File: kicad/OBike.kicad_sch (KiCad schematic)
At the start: 48 parts, among them J1 Conn_01x08, J2 Micro_SD_Card_Det1, J3 Conn_01x02, J4 2337019-1, J6 Conn_01x02, SW1 5_position_tactile, U1 DPS368XTSA1, U2 DS3231M, U3 MCP23017_SO, U4 74HC14, U5 Seeed Studio XIAO SAMD21, U6 MAX-M8C-0

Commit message: gps 4-layer
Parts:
- removed J4: 2337019-1, TE Connectivity:TE_2337019-1, symbol TE Connectivity:2337019-1
- added AE1: Antenna, Antenna:AC30036-01, symbol Device:Antenna
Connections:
- net ANT: now also AE1.1 (A)
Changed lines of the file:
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@@
 	(wire
 		(pts
-			(xy 96.52 102.87) (xy 99.06 102.87)
+			(xy 96.52 110.49) (xy 99.06 110.49)
 		)
 		(stroke
@@
 	(wire
 		(pts
-			(xy 99.06 105.41) (xy 99.06 107.95)
-		)
-		(stroke
-			(width 0)
-			(type default)
-		)
-	)
-	(wire
-		(pts
 			(xy 195.58 33.02) (xy 193.04 33.02)
 		)
@@
 	(wire
 		(pts
-			(xy 96.52 105.41) (xy 99.06 105.41)
-		)
-		(stroke
-			(width 0)
-			(type default)
-		)
-	)
-	(wire
-		(pts
 			(xy 247.65 146.05) (xy 247.65 160.02)
 		)
@@
 	(global_label "ANT"
 		(shape input)
-		(at 99.06 102.87 0)
+		(at 99.06 110.49 0)
 		(fields_autoplaced yes)
 		(effects
@@
 		)
 		(property "Intersheetrefs" "${INTERSHEET_REFS}"
-			(at 105.4319 102.87 0)
+			(at 105.4319 110.49 0)
 			(effects
 				(font
@@
 	)
 	(symbol
-		(lib_id "power:Earth")
-		(at 99.06 107.95 0)
-		(unit 1)
-		(exclude_from_sim no)
-		(in_bom yes)
-		(on_board yes)
-		(dnp no)
-		(property "Reference" "#PWR019"
-			(at 99.06 114.3 0)
-			(effects
-				(font
-					(size 1.27 1.27)
-				)
-				(hide yes)
-			)
-		)
-		(property "Value" "GND"
-			(at 101.6 109.2199 0)
-			(effects
-				(font
-					(size 1.27 1.27)
-				)
-				(justify left)
-			)
-		)
-		(property "Footprint" ""
-			(at 99.06 107.95 0)
-			(effects
-				(font
-					(size 1.27 1.27)
-				)
-				(hide yes)
-			)
-		)
-		(property "Datasheet" "~"
-			(at 99.06 107.95 0)
-			(effects
-				(font
-					(size 1.27 1.27)
-				)
-				(hide yes)
-			)
-		)
-		(property "Description" "Power symbol creates a global label with name \"Earth\""
-			(at 99.06 107.95 0)
-			(effects
-				(font
-					(size 1.27 1.27)
-				)
-				(hide yes)
-			)
-		)
-		(pin "1"
-		)
-		(instances
-			(project "OBike"
-				(path "/b6c91502-91b9-44d0-9569-7774925b5f71"
-					(reference "#PWR019")
-					(unit 1)
-				)
-			)
-		)
-	)
-	(symbol
 		(lib_id "Device:R")
 		(at 199.39 36.83 270)
@@
 	)
 	(symbol
+		(lib_id "Device:Antenna")
+		(at 91.44 110.49 90)
+		(unit 1)
+		(exclude_from_sim no)
+		(in_bom yes)
+		(on_board yes)
+		(dnp no)
+		(fields_autoplaced yes)
+		(property "Reference" "AE1"
+			(at 92.075 104.14 90)
+			(effects
+				(font
+					(size 1.27 1.27)
+				)
+			)
+		)
+		(property "Value" "Antenna"
+			(at 92.075 106.68 90)
+			(effects
+				(font
+					(size 1.27 1.27)
+				)
+			)
+		)
+		(property "Footprint" "Antenna:AC30036-01"
+			(at 91.44 110.49 0)
+			(effects
+				(font
+					(size 1.27 1.27)
+				)
+				(hide yes)
+			)
+		)
+		(property "Datasheet" "~"
+			(at 91.44 110.49 0)
+			(effects
+				(font
+					(size 1.27 1.27)
+				)
+				(hide yes)
+			)
+		)
+		(property "Description" "Antenna"
+			(at 91.44 110.49 0)
+			(effects
+				(font
+					(size 1.27 1.27)
+				)
+				(hide yes)
+			)
+		)
+		(pin "1"
+		)
+		(instances
+			(project ""
+				(path "/b6c91502-91b9-44d0-9569-7774925b5f71"
+					(reference "AE1")
+					(unit 1)
+				)
+			)
+		)
+	)
+	(symbol
 		(lib_id "Device:R")
 		(at 193.04 27.94 0)
@@
 					(unit 1)
 				)
-			)
-		)
-	)
-	(symbol
-		(lib_id "TE Connectivity:2337019-1")
-		(at 93.98 102.87 0)
-		(unit 1)
-		(exclude_from_sim no)
-		(in_bom yes)
-		(on_board yes)
-		(dnp no)
-		(fields_autoplaced yes)
-		(property "Reference" "J4"
-			(at 92.9005 96.52 0)
-			(effects
-				(font
-					(size 1.27 1.27)
-				)
-			)
-		)
-		(property "Value" "2337019-1"
-			(at 92.9005 99.06 0)
-			(effects
-				(font
-					(size 1.27 1.27)
-				)
-			)
-		)
-		(property "Footprint" "TE Connectivity:TE_2337019-1"
-			(at 93.98 102.87 0)
-			(effects
-				(font
-					(size 1.27 1.27)
-				)
-				(justify bottom)
-				(hide yes)
-			)
-		)
-		(property "Datasheet" ""
-			(at 93.98 102.87 0)
-			(effects
-				(font
-					(size 1.27 1.27)
-				)
-				(hide yes)
-			)
-		)
-		(property "Description" ""
-			(at 93.98 102.87 0)
-			(effects
-				(font
-					(size 1.27 1.27)
-				)
-				(hide yes)
-			)
-		)
-		(property "PARTREV" "A4"
-			(at 93.98 102.87 0)
-			(effects
-				(font
-					(size 1.27 1.27)
-				)
-				(justify bottom)
-				(hide yes)
-			)
-		)
-		(property "STANDARD" "Manufacturer Recommendations"
-			(at 93.98 102.87 0)
-			(effects
-				(font
-					(size 1.27 1.27)
-				)
-				(justify bottom)
-				(hide yes)
-			)
-		)
-		(property "MAXIMUM_PACKAGE_HEIGHT" "1.25mm"
-			(at 93.98 102.87 0)
-			(effects
-				(font
-					(size 1.27 1.27)
-				)
-				(justify bottom)
-				(hide yes)
-			)
-		)
-		(property "MANUFACTURER" "TE Connectivity"
-			(at 93.98 102.87 0)
-			(effects
-				(font
-					(size 1.27 1.27)
-				)
-				(justify bottom)
-				(hide yes)
-			)
-		)
-		(pin "G1"
-		)
-		(pin "1"
-		)
-		(instances
-			(project ""
-				(path "/b6c91502-91b9-44d0-9569-7774925b5f71"
-					(reference "J4")
-					(unit 1)
-				)

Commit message: stopper using logger
also some fixes for tcx
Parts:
- added R15, R17: 100K, Resistor_SMD:R_0603_1608Metric, symbol Device:R
- AE1: Digikiey PN (none) -> 5350-AC30036-01-ND; Manufacturer (none) -> The Antenna Company; Manufacturer PN (none) -> AC30036-01
- D1, D2, D3, D4, D5: Digikiey PN (none) -> 1N4148WRHGCT-ND; Manufacturer (none) -> Taiwan Semiconductor Corporation; Manufacturer PN (none) -> 1N4148W RHG
- J2: Digikiey PN (none) -> 2223-MSD-11-ACT-ND; Manufacturer (none) -> Same Sky (Formerly CUI Devices); Manufacturer PN (none) -> MSD-11-A
- J3: Digikiey PN (none) -> 455-1719-ND; Manufacturer (none) -> JST Sales America Inc.; Manufacturer PN (none) -> CONN HEADER R/A 2POS 2MM
- R16: value 10K -> 100K
- SW1: Digikiey PN (none) -> 450-2425755-1CT-ND; Manufacturer (none) -> TE Connectivity ALCOSWITCH Switches; Manufacturer PN (none) -> 2425755-1
- U1: Digikiey PN (none) -> DPS368XTSA1CT-ND; Manufacturer (none) -> Infineon Technologies; Manufacturer PN (none) -> DPS368XTSA1
- U2: Digikiey PN (none) -> DS3231MZ+-ND; Manufacturer (none) -> Analog Devices Inc./Maxim Integrated; Manufacturer PN (none) -> DS3231MZ+
- U3: Digikiey PN (none) -> MCP23017T-E/SOCT-ND; Manufacturer (none) -> Microchip Technology; Manufacturer PN (none) -> MCP23017T-E/SO
- U4: Digikiey PN (none) -> 74HC14DCT-ND; Manufacturer (none) -> Toshiba Semiconductor and Storage; Manufacturer PN (none) -> 74HC14D
- U6: Digikiey PN (none) -> 672-MAX-M8C-0CT-ND; MANUFACTURER u-blox -> (none); Manufacturer (none) -> u-blox; Manufacturer PN (none) -> MAX-M8C-0
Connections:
- net at C10.1, J2.1 (DAT2), R11.1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: now also R15.1, R17.1; no longer J2.4 (VDD), J2.8 (DAT1)
- new net: J2.4 (VDD), R15.2
- new net: J2.8 (DAT1), R17.2

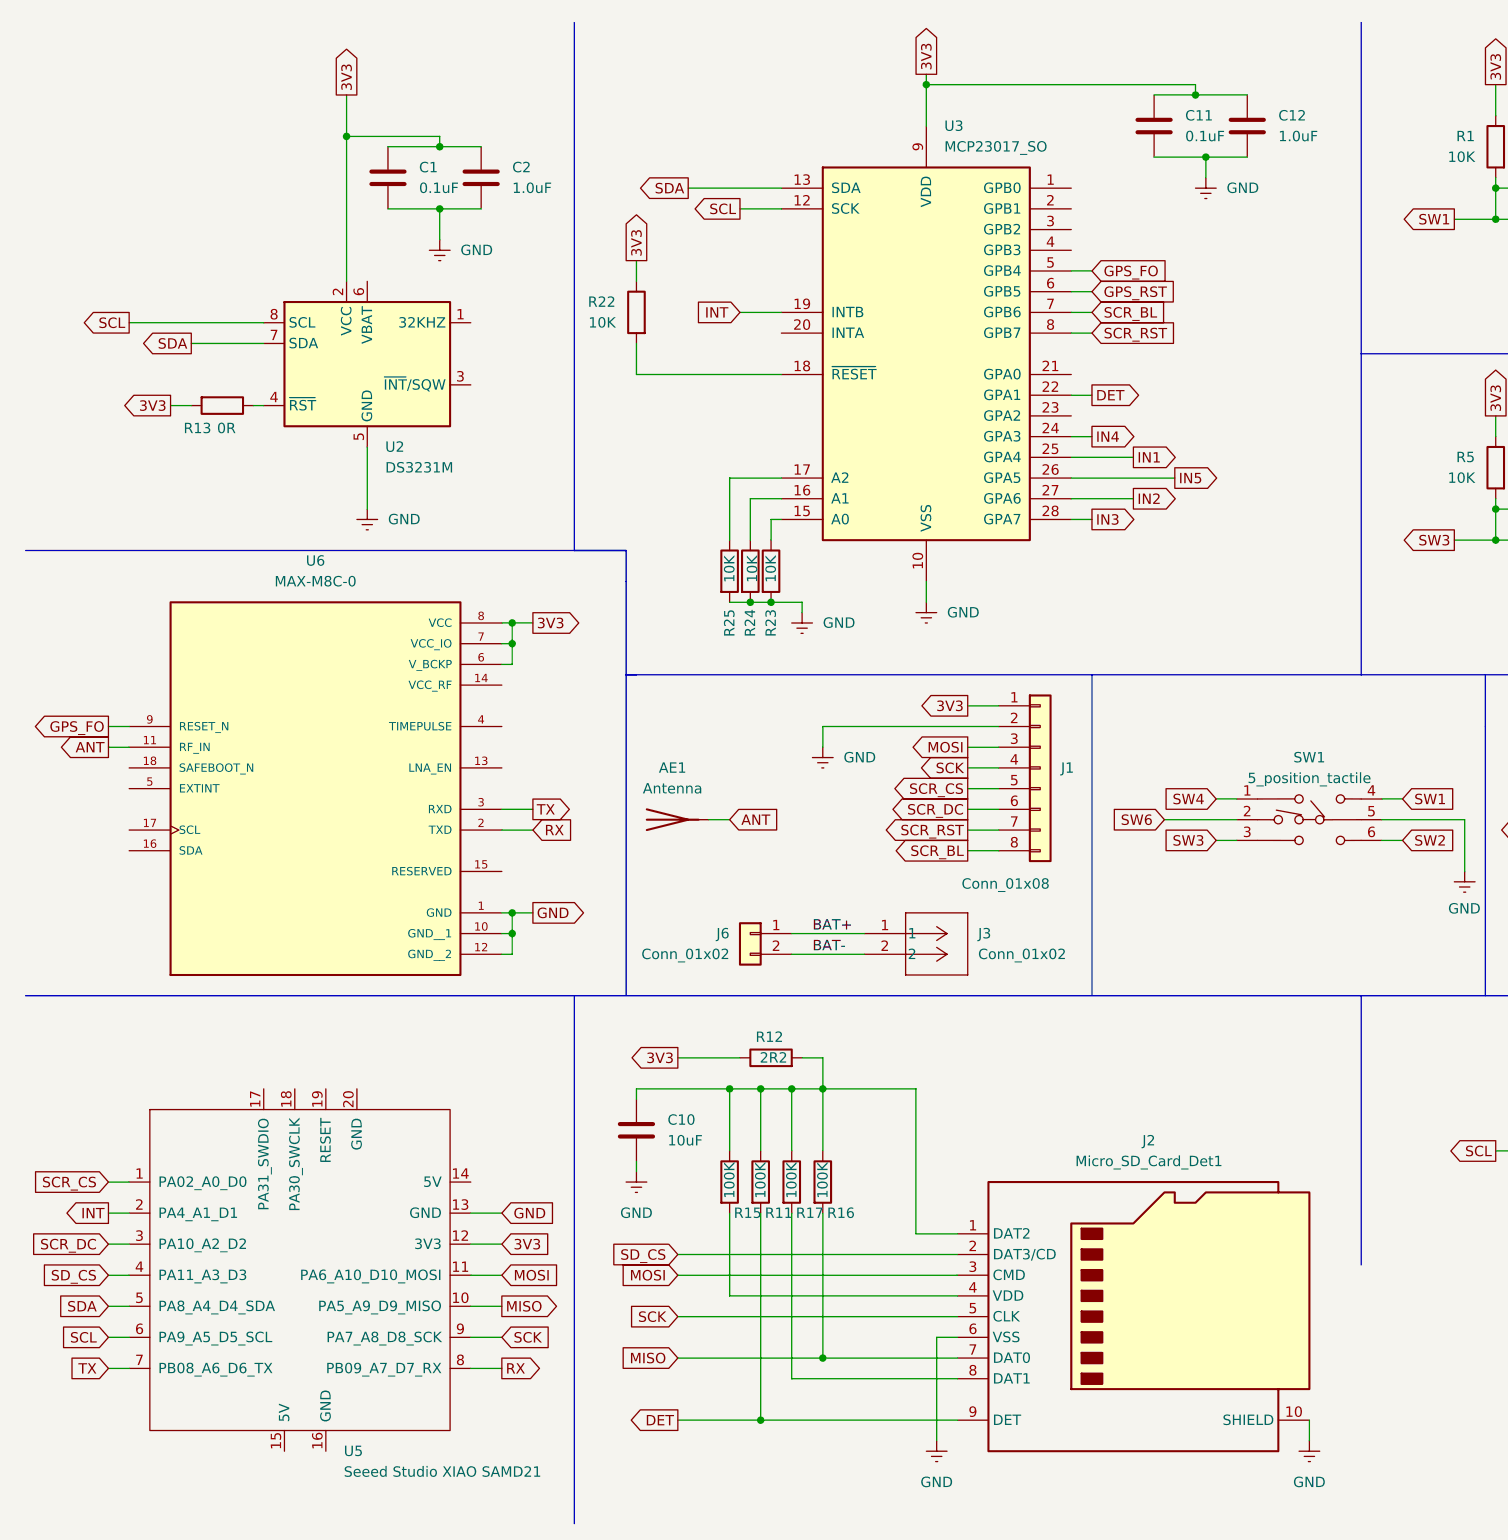
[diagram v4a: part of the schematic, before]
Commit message: quectel module
changed gps module
increased board size
moved gps module to front bottom left
moved sd card front bottom right
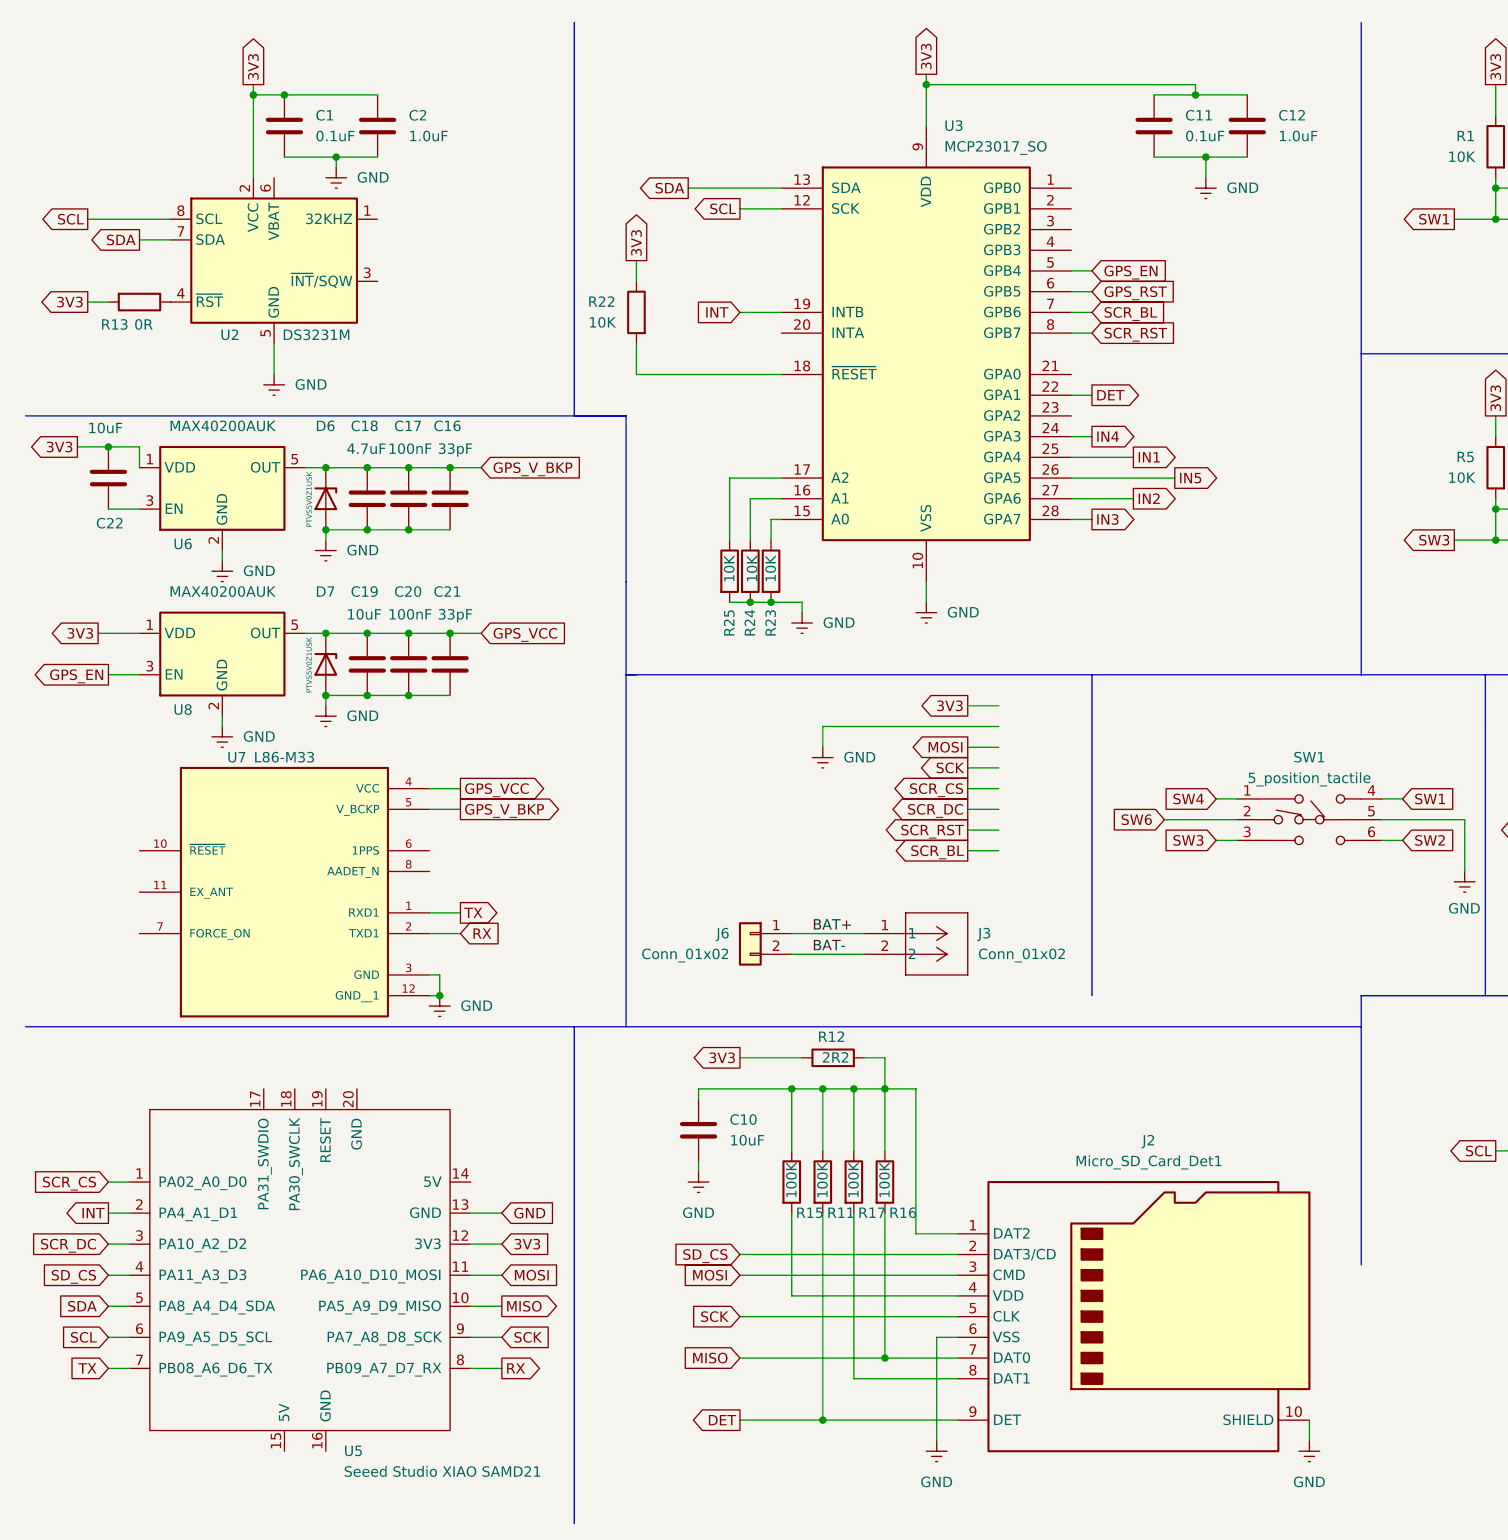
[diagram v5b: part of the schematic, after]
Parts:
- removed AE1: Antenna, Antenna:AC30036-01, symbol Device:Antenna
- removed J1: Conn_01x08, Connector_JST:JST_GH_SM08B-GHS-TB_1x08-1MP_P1.25mm_Horizontal, symbol Connector_Generic:Conn_01x08
- removed U6: MAX-M8C-0, uBlox:XCVR_MAX-M8C-0, symbol uBlox:MAX-M8C-0
- added C16, C21: 33pF, Capacitor_SMD:C_0603_1608Metric, symbol Device:C
- added C17, C20: 100nF, Capacitor_SMD:C_0603_1608Metric, symbol Device:C
- added C18: 4.7uF, Capacitor_SMD:C_0603_1608Metric, symbol Device:C
- added C19, C22: 10uF, Capacitor_SMD:C_0603_1608Metric, symbol Device:C
- added D6, D7: PTVS5V0Z1USK, Diode_SMD:Nexperia_DSN1608-2_1.6x0.8mm, symbol Diode:PTVS5V0Z1USK
- added U6, U8: MAX40200AUK, Package_TO_SOT_SMD:SOT-23-5, symbol Analog_Switch:MAX40200AUK
- added U7: L86-M33, quectel:L86-M33, symbol quectel:L86-M33
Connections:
- net 3V3: now also C22.1, U6.1 (VDD), U8.1 (VDD)
- net GND: now also C16.2, C17.2, C18.2, C19.2, C20.2, C21.2, D6.2 (A), D7.2 (A), U6.2 (GND), U7.12 (GND__1), U7.3 (GND), U8.2 (GND)
- net RX: now also U7.2 (TXD1)
- net TX: now also U7.1 (RXD1)
- net GPS_FO renamed GPS_EN
- net GPS_EN: now also U8.3 (EN)
- new net: C22.2, U6.3 (EN)
- new net GPS_VCC: C19.1, C20.1, C21.1, D7.1 (K), U7.4 (VCC), U8.5 (OUT)
- new net GPS_V_BKP: C16.1, C17.1, C18.1, D6.1 (K), U6.5 (OUT), U7.5 (V_BCKP)
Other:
- moved on the sheet: C1, C10, C2, R11, R12, R13, R15, R16, R17, U2

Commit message: rev 3 pcb
- quectel gps
- u.fl antenae conn
- aux power switch
- flash chip
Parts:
- removed C22: 10uF, Capacitor_SMD:C_0603_1608Metric, symbol Device:C
- removed U7: L86-M33, quectel:L86-M33, symbol quectel:L86-M33
- added J1: 62684-402100ALF, amphenol:AMPHENOL_62684-402100ALF, symbol amphenol:62684-402100ALF
- added J5: U.FL-R-SMT-1_10_, Hirose:HRS_U.FL-R-SMT-1_10_, symbol Hirose:U.FL-R-SMT-1_10_
- added U10: MAX40200AUK, Package_TO_SOT_SMD:SOT-23-5, symbol Analog_Switch:MAX40200AUK
- added U7: LC76G, quectel:XCVR_LC76G, symbol LC76G:LC76G
- added U9: W25N01GVZEIG_TR, windbond:SON127P800X600X80-9N, symbol Windbond:W25N01GVZEIG_TR
- J2: footprint CUI-devices:CUI_MSD-11-A -> CUI:CUI_MSD-4-A
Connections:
- net 3V3: now also U10.1 (VDD); no longer C3.1, C4.1, R12.1, U1.6 (VDDIO), U1.8 (VDD)
- net GND: now also J1.05, J1.16, J1.37, J1.S1 (SHIELD), J1.S2 (SHIELD__1), J5.1, J5.3, U10.2 (GND), U7.1 (GND), U7.10 (GND__1), U7.12 (GND__2), U7.28 (GND__3), U9.4 (GND)
- net GPS_EN: now also U3.4 (GPB3); no longer U3.5 (GPB4)
- net GPS_RST: now also U7.9 (~{RESET})
- net GPS_VCC: now also U7.8 (VCC)
- net GPS_V_BKP: now also U7.6 (V_BCKP)
- net MISO: now also J1.14, U9.2 (DO(IO1))
- net MOSI: now also J1.13, U9.5 (DI(IO0))
- net SCK: now also J1.10, U9.6 (CLK)
- net SCL: now also U7.17 (I2C_SCL)
- net SCR_CS: now also J1.09
- net SCR_DC: now also J1.11
- net SDA: now also U7.16 (I2C_SDA)
- net GPS_BKP: now reaches U6.3 (EN)
- net GPS_BKP: now also U3.5 (GPB4)
- net CD: now reaches U3.23 (GPA2)
- net CD: now also J2.9 (CD), R11.2
- removed net DET: J2.9 (DET), R11.2, U3.22 (GPA1)
- net RX renamed FL_CS
- net FL_CS: now also U9.1 (/CS)
- net TX renamed AUX_EN
- net AUX_EN: now also U10.3 (EN)
- new net ANT: J5.2, U7.11 (RF_IN)
- new net AUX_3V3: C3.1, C4.1, J1.07, R12.1, U1.6 (VDDIO), U1.8 (VDD), U10.5 (OUT), U9.8 (VCC)
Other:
- moved on the sheet: C1, C10, C11, C12, C16, C17, C18, C19, C2, C20, C21, C3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
